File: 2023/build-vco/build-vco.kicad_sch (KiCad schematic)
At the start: 26 parts, among them M1 PMOS_OR1, M10 NMOS_OR1, M11 NMOS_OR1, M12 NMOS_OR1, M13 PMOS_OR1, M14 PMOS_OR1, M15 NMOS_OR1, M16 NMOS_OR1, M17 PMOS_OR1, M18 NMOS_OR1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

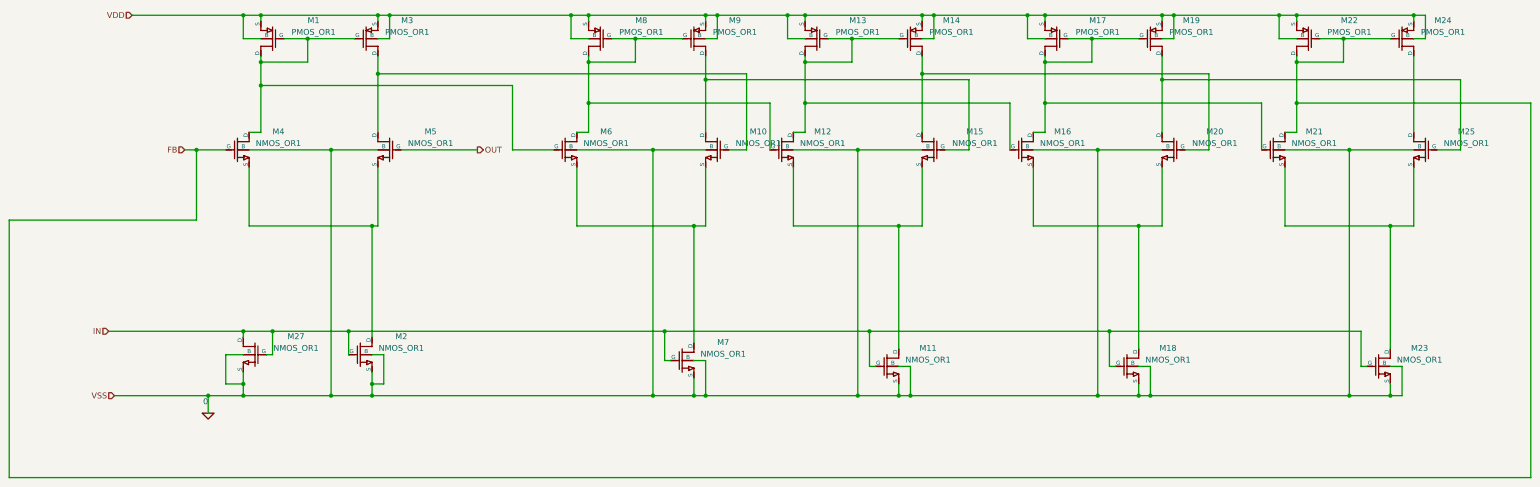
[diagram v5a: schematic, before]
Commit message: とりあえず完成して、DRC, LVS OK.
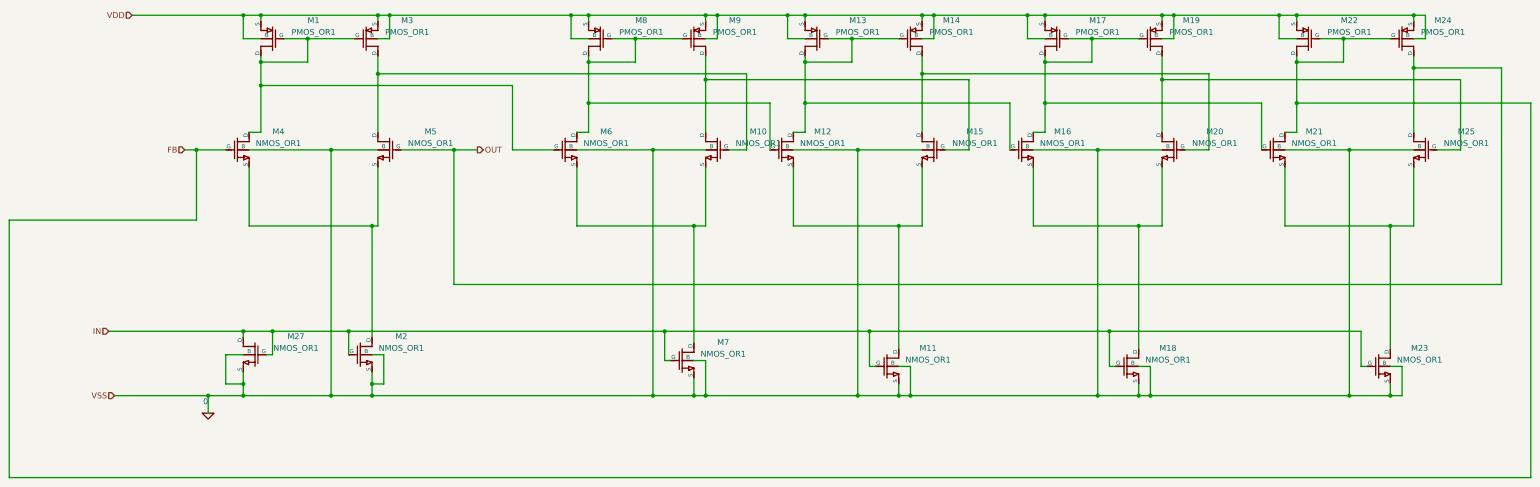
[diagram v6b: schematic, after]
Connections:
- net OUT: now also M24.1 (D), M25.1 (D)
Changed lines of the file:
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@@
   (junction (at 279.4 63.5) (diameter 0) (color 0 0 0 0)
   )
+  (junction (at 96.52 92.71) (diameter 0) (color 0 0 0 0)
+  )
   (junction (at 64.77 68.58) (diameter 0) (color 0 0 0 0)
   )
@@
   (junction (at 184.15 92.71) (diameter 0) (color 0 0 0 0)
   )
+  (junction (at 304.8 74.93) (diameter 0) (color 0 0 0 0)
+  )
   (junction (at 139.7 92.71) (diameter 0) (color 0 0 0 0)
   )
@@
     (stroke (width 0) (type default))
   )
+  (wire (pts (xy 96.52 92.71) (xy 101.6 92.71))
+    (stroke (width 0) (type default))
+  )
   (wire (pts (xy 78.74 109.22) (xy 80.01 109.22))
     (stroke (width 0) (type default))
@@
     (stroke (width 0) (type default))
   )
+  (wire (pts (xy 323.85 74.93) (xy 323.85 121.92))
+    (stroke (width 0) (type default))
+  )
   (wire (pts (xy 177.8 68.58) (xy 182.88 68.58))
     (stroke (width 0) (type default))
@@
     (stroke (width 0) (type default))
   )
-  (wire (pts (xy 85.09 92.71) (xy 101.6 92.71))
+  (wire (pts (xy 85.09 92.71) (xy 96.52 92.71))
     (stroke (width 0) (type default))
   )
@@
     (stroke (width 0) (type default))
   )
+  (wire (pts (xy 323.85 121.92) (xy 96.52 121.92))
+    (stroke (width 0) (type default))
+  )
   (wire (pts (xy 40.64 92.71) (xy 40.64 107.95))
     (stroke (width 0) (type default))
@@
     (stroke (width 0) (type default))
   )
+  (wire (pts (xy 304.8 74.93) (xy 323.85 74.93))
+    (stroke (width 0) (type default))
+  )
   (wire (pts (xy 184.15 92.71) (xy 198.12 92.71))
     (stroke (width 0) (type default))
@@
     (stroke (width 0) (type default))
   )
+  (wire (pts (xy 304.8 74.93) (xy 304.8 88.9))
+    (stroke (width 0) (type default))
+  )
   (wire (pts (xy 168.91 63.5) (xy 172.72 63.5))
     (stroke (width 0) (type default))
@@
     (stroke (width 0) (type default))
   )
-  (wire (pts (xy 304.8 72.39) (xy 304.8 88.9))
+  (wire (pts (xy 304.8 72.39) (xy 304.8 74.93))
     (stroke (width 0) (type default))
   )
@@
     (stroke (width 0) (type default))
   )
+  (wire (pts (xy 96.52 121.92) (xy 96.52 92.71))
+    (stroke (width 0) (type default))
+  )
